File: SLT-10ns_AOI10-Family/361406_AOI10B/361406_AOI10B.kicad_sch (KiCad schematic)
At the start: 20 parts, among them T1 IBM_Transistor, T2 IBM_Transistor

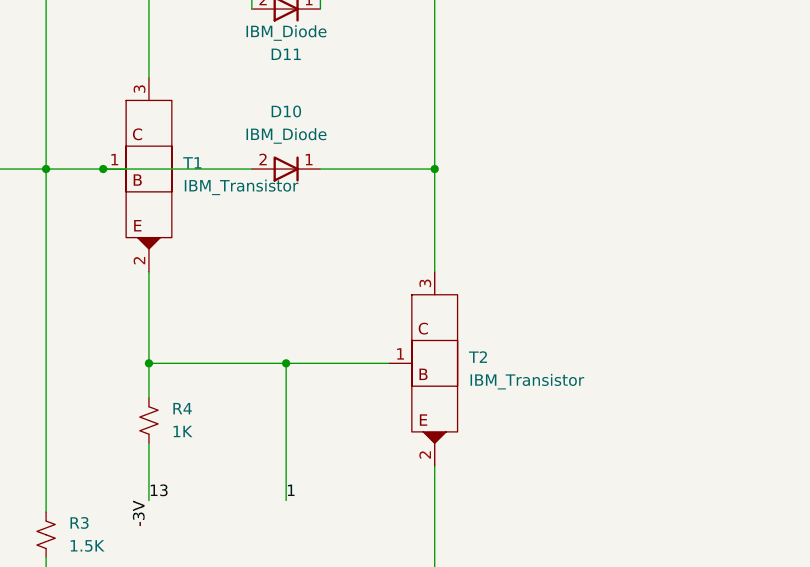
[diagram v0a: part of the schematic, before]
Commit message: Finished off the SLT-30 family of parts, started on the SLT-700 family. Changed labeling of transistors and diodes in all schematics, but have yet to update all the pdf files. This is a TODO...
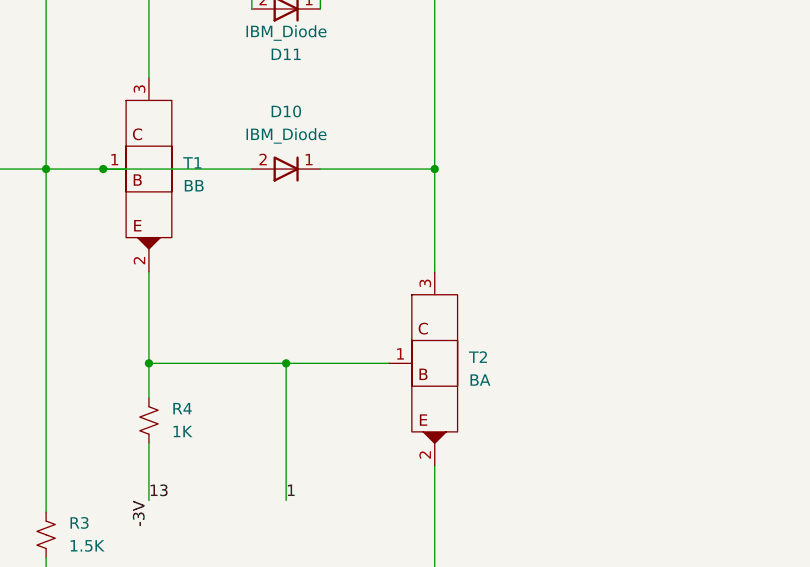
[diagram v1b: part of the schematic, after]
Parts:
- T1: value IBM_Transistor -> BB
- T2: value IBM_Transistor -> BA
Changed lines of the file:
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@@
       (effects (font (size 1.27 1.27)) (justify left))
     )
-    (property "Value" "IBM_Transistor" (id 1) (at 156.21 117.4749 0)
+    (property "Value" "BA" (id 1) (at 156.21 117.4749 0)
       (effects (font (size 1.27 1.27)) (justify left))
     )
@@
       (effects (font (size 1.27 1.27)) (justify left))
     )
-    (property "Value" "IBM_Transistor" (id 1) (at 124.46 95.8849 0)
+    (property "Value" "BB" (id 1) (at 124.46 95.8849 0)
       (effects (font (size 1.27 1.27)) (justify left))
     )
@@
     )
     (path "/a58b425b-6fc3-4a86-ae11-a84decf83c5a"
-      (reference "T1") (unit 1) (value "IBM_Transistor") (footprint "")
+      (reference "T1") (unit 1) (value "BB") (footprint "")
     )
     (path "/2873e490-c9bf-4c89-897a-2c4ba6a0f218"
-      (reference "T2") (unit 1) (value "IBM_Transistor") (footprint "")
+      (reference "T2") (unit 1) (value "BA") (footprint "")
     )
     (path "/98cf94aa-9a14-4efb-965e-894e721f61fd"
